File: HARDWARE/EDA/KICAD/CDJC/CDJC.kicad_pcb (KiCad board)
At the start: 2 copper layers, 100 x 100 mm, 55 parts, among them J1 COM_IN, J2 COM_OUT, J3 POWER_IN, J4 POWER_OUT, J5 BIT_OUT, Q1 BC549, SW1 B-SET, U1 74LS04, U2 74LS32, U3 74LS08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

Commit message: pause work0
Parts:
- D10: footprint Diode_THT:D_DO-34_SOD68_P7.62mm_Horizontal -> Diode_THT:D_DO-34_SOD68_P10.16mm_Horizontal
- D11: footprint Diode_THT:D_DO-34_SOD68_P7.62mm_Horizontal -> Diode_THT:D_DO-34_SOD68_P12.70mm_Horizontal
- D20, D21, D9: footprint Diode_THT:D_DO-34_SOD68_P2.54mm_Vertical_AnodeUp -> Diode_THT:D_DO-34_SOD68_P7.62mm_Horizontal
- R10, R12, R13, R14, R15, R16, R7: footprint Resistor_THT:R_Axial_DIN0207_L6.3mm_D2.5mm_P2.54mm_Vertical -> Resistor_THT:R_Axial_DIN0207_L6.3mm_D2.5mm_P7.62mm_Horizontal
- moved U4 46.6 mm to (164.1, 106.8), turned to 270 degrees
- moved U9 44.0 mm to (223.0, 106.2), turned to 270 degrees
- moved D21 38.6 mm to (218.0, 95.9)
- moved SW1 24.5 mm to (124.5, 98.6)
- moved R1 24.5 mm to (128.8, 110.1)
- moved R2 24.5 mm to (128.8, 105.3)
- moved R4 24.5 mm to (130.8, 112.5)
- moved R5 24.5 mm to (130.8, 107.7)
- moved R6 24.5 mm to (130.8, 102.9)
- moved D1 24.5 mm to (123.3, 111.7)
- moved D2 24.5 mm to (123.3, 107.2)
- moved D3 24.5 mm to (123.3, 102.6)
- moved D10 22.2 mm to (208.7, 126.6), turned to 90 degrees
- moved D11 21.6 mm to (225.0, 116.5)
- moved R13 21.3 mm to (177.7, 137.8)
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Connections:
- U4 pad 10: Net-(U1-Pad8) -> Net-(U4-Pad10)
- U4 pad 6: Net-(U4-Pad6) -> Net-(U4-Pad10)
- U4 pad 9: Net-(U4-Pad6) -> Net-(U1-Pad8)
- U7 pad 10: FBMon -> NBMon
- U7 pad 9: NBMon -> FBMon
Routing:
- net LBMon: track 1.04 -> 78.0 mm, vias 0 -> 2
- net +5VD: track 174.2 -> 105.5 mm, vias 6 -> 2
- net Net-(D21-Pad1): track 0.07 -> 61.7 mm
- net LB_SW: track 167.6 -> 120.6 mm, vias 2 -> 4
- net FBMon: track 0.00 -> 46.4 mm, vias 0 -> 2
- net MRLMon: track 0.00 -> 43.6 mm, vias 0 -> 2
- net Net-(U1-Pad8): track 37.5 -> 0.00 mm
- net Net-(U6-Pad3): track 0.00 -> 35.8 mm, vias 0 -> 2
- net NB_SW: track 80.5 -> 45.1 mm, vias 2 -> 0
- net Net-(D16-Pad2): track 0.00 -> 30.2 mm
- net Net-(U5-Pad3): track 0.00 -> 30.0 mm, vias 0 -> 2
- net LBLBI: track 116.8 -> 145.7 mm
- net Net-(U1-Pad4): track 36.9 -> 8.99 mm
- net Net-(D17-Pad2): track 0.00 -> 27.4 mm
- net Net-(D13-Pad1): track 0.00 -> 26.1 mm
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
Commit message: i am crazy
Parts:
- R1, R2, R3, R4, R5, R6: footprint Resistor_THT:R_Axial_DIN0207_L6.3mm_D2.5mm_P2.54mm_Vertical -> Resistor_THT:R_Axial_DIN0207_L6.3mm_D2.5mm_P7.62mm_Horizontal
- moved SW1 67.5 mm to (171.8, 50.4), turned to 270 degrees
- moved R4 58.0 mm to (173.5, 73.2)
- moved R6 58.0 mm to (173.5, 63.6)
- moved R5 58.0 mm to (173.5, 68.4)
- moved R3 54.8 mm to (165.9, 61.2), turned to 0 degrees
- moved D2 54.0 mm to (160.4, 67.9)
- moved R1 54.0 mm to (165.8, 70.8)
- moved R2 54.0 mm to (165.8, 66.0)
- moved D1 54.0 mm to (160.4, 72.4)
- moved D3 54.0 mm to (160.4, 63.3)
- moved U1 32.5 mm to (177.7, 115.4), turned to 90 degrees
- moved U4 15.3 mm to (177.7, 99.9), turned to 90 degrees
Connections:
- U1 pad 11: FB_SW -> NB_SW
- U1 pad 13: NB_SW -> LB_SW
- U1 pad 9: LB_SW -> FB_SW
- U2 pad 12: NB_SW -> LB_SW
- U2 pad 13: LB_SW -> NB_SW
- U2 pad 6: Net-(U1-Pad1) -> Net-(U1-Pad5)
- U2 pad 8: Net-(U1-Pad5) -> Net-(U1-Pad1)
- U3 pad 1: GNDD -> LB_SW
- U3 pad 10: FB_SW -> Net-(D10-Pad1)
- U3 pad 11: LBMon -> FBMon
- U3 pad 12: LB_SW -> FB_SW
- U3 pad 13: Net-(U1-Pad2) -> Net-(U1-Pad4)
- U3 pad 2: GNDD -> Net-(U1-Pad6)
- U3 pad 3: Net-(U3-Pad3) -> LBMon
- U3 pad 4: Net-(U1-Pad6) -> Net-(U1-Pad2)
- U3 pad 8: FBMon -> Net-(U3-Pad8)
- U3 pad 9: Net-(U1-Pad4) -> MRLMon
- U4 pad 4: Net-(U1-Pad12) -> Net-(U1-Pad10)
- U4 pad 5: Net-(U1-Pad10) -> Net-(U1-Pad8)
- U4 pad 9: Net-(U1-Pad8) -> Net-(U1-Pad12)
- U6 pad 1: Net-(D10-Pad1) -> GNDD
- U6 pad 2: MRLMon -> GNDD
- U8 pad 2: Net-(U6-Pad3) -> Net-(U3-Pad8)
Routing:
- net Net-(U1-Pad1): track 0.00 -> 91.0 mm, vias 0 -> 2
- net Net-(U1-Pad3): track 0.00 -> 68.9 mm
- net Net-(U1-Pad6): track 6.98 -> 67.8 mm, vias 0 -> 2
- net Net-(U1-Pad5): track 0.06 -> 56.5 mm
- net Net-(U1-Pad4): track 8.99 -> 63.5 mm, vias 0 -> 2
- net NB_SW: track 45.1 -> 96.6 mm, vias 0 -> 2
- net GNDD: track 208.7 -> 257.7 mm, vias 6 -> 10
- net NBMon: track 15.4 -> 58.0 mm, vias 0 -> 2
- net Net-(U6-Pad3): track 35.8 -> 0.00 mm, vias 2 -> 0
- net LBMon: track 78.0 -> 110.4 mm, vias 2 -> 6
- net Net-(U3-Pad8): track 0.00 -> 25.3 mm, vias 0 -> 2
- net Net-(U1-Pad2): track 26.2 -> 48.1 mm, vias 0 -> 2
- net FB_SW: track 71.9 -> 91.9 mm
- net Net-(U1-Pad12): track 14.2 -> 31.9 mm, vias 0 -> 2
- net Net-(U1-Pad8): track 0.00 -> 9.98 mm
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
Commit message: i am crazy
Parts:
- moved U1 15.9 mm to (193.4, 112.9), turned to 180 degrees
- moved R3 13.9 mm to (152.1, 62.7)
- moved R5 13.9 mm to (159.7, 69.9)
- moved SW1 13.9 mm to (158.0, 51.9)
- moved D1 13.9 mm to (146.6, 73.9)
- moved D2 13.9 mm to (146.6, 69.4)
- moved D3 13.9 mm to (146.6, 64.8)
- moved R1 13.9 mm to (152.1, 72.3)
- moved R2 13.9 mm to (152.1, 67.5)
- moved R4 13.9 mm to (159.7, 74.7)
- moved R6 13.9 mm to (159.7, 65.1)
- moved U4 13.6 mm to (173.4, 112.8), turned to 180 degrees
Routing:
- net LB_SW: track 119.3 -> 28.3 mm, vias 4 -> 0
- net Net-(U1-Pad1): track 91.0 -> 0.00 mm, vias 2 -> 0
- net NB_SW: track 96.6 -> 24.4 mm, vias 2 -> 0
- net Net-(U1-Pad3): track 68.9 -> 0.00 mm
- net Net-(U1-Pad6): track 67.8 -> 0.00 mm, vias 2 -> 0
- net LBMon: track 110.4 -> 45.8 mm, vias 6 -> 2
- net Net-(U1-Pad4): track 63.5 -> 0.00 mm, vias 2 -> 0
- net Net-(U1-Pad5): track 56.5 -> 0.00 mm
- net Net-(U1-Pad2): track 48.1 -> 0.00 mm, vias 2 -> 0
- net MRLMon: track 44.0 -> 0.00 mm
- net NBMon: track 58.0 -> 15.4 mm, vias 2 -> 0
- net Net-(U1-Pad12): track 31.9 -> 0.00 mm, vias 2 -> 0
- net FB_SW: track 91.9 -> 63.9 mm, vias 4 -> 2
- net Net-(U1-Pad8): track 9.98 -> 0.00 mm
- net Net-(U1-Pad10): track 8.93 -> 0.00 mm
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
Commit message: ajdust PCB
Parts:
- moved R5 51.4 mm to (178.4, 117.8)
- moved D1 51.4 mm to (165.3, 121.8)
- moved D2 51.4 mm to (165.3, 117.3)
- moved D3 51.4 mm to (165.3, 112.7)
- moved R1 51.4 mm to (170.8, 120.2)
- moved R2 51.4 mm to (170.8, 115.4)
- moved R3 51.4 mm to (170.8, 110.6)
- moved R4 51.4 mm to (178.4, 122.6)
- moved R6 51.4 mm to (178.4, 113.0)
- moved SW1 48.9 mm to (170.9, 99.1)
- moved U4 43.9 mm to (171.3, 69.0)
- moved U3 36.8 mm to (194.8, 115.8), turned to 180 degrees
- moved U1 25.7 mm to (190.4, 87.4)
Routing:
- net FB_SW: track 63.9 -> 8.67 mm, vias 2 -> 0
- net FBMon: track 56.3 -> 18.2 mm
- net LB_SW: track 28.3 -> 10.3 mm
- net NB_SW: track 24.4 -> 11.9 mm
- net Net-(U3-Pad8): track 25.3 -> 14.5 mm, vias 2 -> 1

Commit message: remaining editions
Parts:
- moved R1 48.0 mm to (167.1, 72.3)
- moved R6 48.0 mm to (174.7, 65.1)
- moved R2 48.0 mm to (167.1, 67.5)
- moved R3 48.0 mm to (167.1, 62.7)
- moved R4 48.0 mm to (174.7, 74.7)
- moved R5 48.0 mm to (174.7, 69.9)
- moved D2 48.0 mm to (162.3, 69.4)
- moved D3 48.0 mm to (162.3, 64.8)
- moved D1 48.0 mm to (162.3, 73.9)
- moved U4 47.6 mm to (172.2, 116.6)
- moved SW1 47.0 mm to (162.6, 52.8), turned to 0 degrees
- moved U2 15.9 mm to (217.9, 89.9), turned to 180 degrees
- moved U1 5.24 mm to (195.0, 89.9)
- moved D4 2.60 mm to (162.7, 133.9)
- moved D5 2.60 mm to (162.7, 130.2)
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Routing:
- net GNDD: track 257.7 -> 230.4 mm, vias 10 -> 8
- net Net-(U5-Pad10): track 42.8 -> 41.8 mm
- net Net-(U6-Pad6): track 45.4 -> 44.6 mm
- net Net-(D1-Pad2): track 2.78 -> 3.61 mm
- net Net-(U6-Pad10): track 27.3 -> 26.7 mm

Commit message: adjusts in PCB
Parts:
- moved U2 71.1 mm to (146.8, 88.8), turned to 0 degrees
- moved U3 35.0 mm to (173.5, 88.9), turned to 0 degrees
- moved U1 34.9 mm to (160.1, 88.8), turned to 0 degrees
- moved U4 31.5 mm to (187.2, 88.9), turned to 0 degrees
- moved D1 1.97 mm to (162.2, 72.0)
- moved R3 1.97 mm to (167.0, 60.7)
- moved R5 1.97 mm to (174.6, 67.9)
- moved D2 1.97 mm to (162.2, 67.4)
- moved R1 1.97 mm to (167.0, 70.3)
- moved R2 1.97 mm to (167.0, 65.5)
- moved R4 1.97 mm to (174.7, 72.7)
- moved R6 1.97 mm to (174.7, 63.1)
- moved D3 1.97 mm to (162.2, 62.9)
- moved SW1 1.38 mm to (162.5, 51.4)
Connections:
- U1 pad 1: Net-(U1-Pad1) -> NB_SW
- U1 pad 11: NB_SW -> Net-(U1-Pad11)
- U1 pad 13: LB_SW -> FB_SW
- U1 pad 5: Net-(U1-Pad5) -> LB_SW
- U1 pad 9: FB_SW -> Net-(U1-Pad9)
- U2 pad 6: Net-(U1-Pad5) -> Net-(U1-Pad9)
- U2 pad 8: Net-(U1-Pad1) -> Net-(U1-Pad11)
- U3 pad 1: LB_SW -> NB_SW
- U3 pad 10: Net-(D10-Pad1) -> Net-(U1-Pad12)
- U3 pad 2: Net-(U1-Pad6) -> Net-(U1-Pad10)
- U3 pad 3: LBMon -> NBMon
- U3 pad 4: Net-(U1-Pad2) -> Net-(U1-Pad8)
- U3 pad 5: NB_SW -> LB_SW
- U3 pad 6: NBMon -> LBMon
- U3 pad 9: MRLMon -> Net-(U1-Pad2)
- U4 pad 1: FB_SW -> NB_SW
- U4 pad 11: MRLMon -> Net-(U4-Pad11)
- U4 pad 12: Net-(U4-Pad12) -> MRLMon
- U4 pad 13: LB_SW -> Net-(D10-Pad1)
- U4 pad 2: NB_SW -> FB_SW
- U4 pad 3: Net-(U4-Pad12) -> Net-(U4-Pad10)
- U4 pad 4: Net-(U1-Pad10) -> Net-(U1-Pad6)
- U4 pad 5: Net-(U1-Pad8) -> Net-(U3-Pad8)
- U4 pad 6: Net-(U4-Pad10) -> ELMon
- U4 pad 8: ELMon -> MRLMon
- U4 pad 9: Net-(U1-Pad12) -> LB_SW
- U8 pad 2: Net-(U3-Pad8) -> Net-(U4-Pad11)
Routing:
- net LB_SW: track 10.3 -> 110.5 mm, vias 0 -> 4
- net FB_SW: track 8.67 -> 92.3 mm
- net +5VD: track 100.7 -> 171.5 mm, vias 2 -> 8
- net NB_SW: track 11.9 -> 70.4 mm, vias 0 -> 4
- net Net-(U1-Pad6): track 0.00 -> 55.9 mm, vias 0 -> 2
- net Net-(U1-Pad2): track 0.00 -> 53.2 mm, vias 0 -> 4
- net Net-(U1-Pad4): track 0.00 -> 41.6 mm, vias 0 -> 2
- net Net-(U1-Pad9): track 0.00 -> 35.1 mm
- net Net-(U1-Pad12): track 0.00 -> 32.0 mm
- net Net-(U1-Pad11): track 0.00 -> 28.7 mm
- net NBMon: track 15.4 -> 32.6 mm
- net Net-(U4-Pad11): track 0.00 -> 14.5 mm, vias 0 -> 1
- net Net-(U1-Pad8): track 0.00 -> 11.3 mm
- net Net-(U4-Pad10): track 0.00 -> 11.1 mm
- net Net-(U1-Pad10): track 0.00 -> 10.7 mm
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
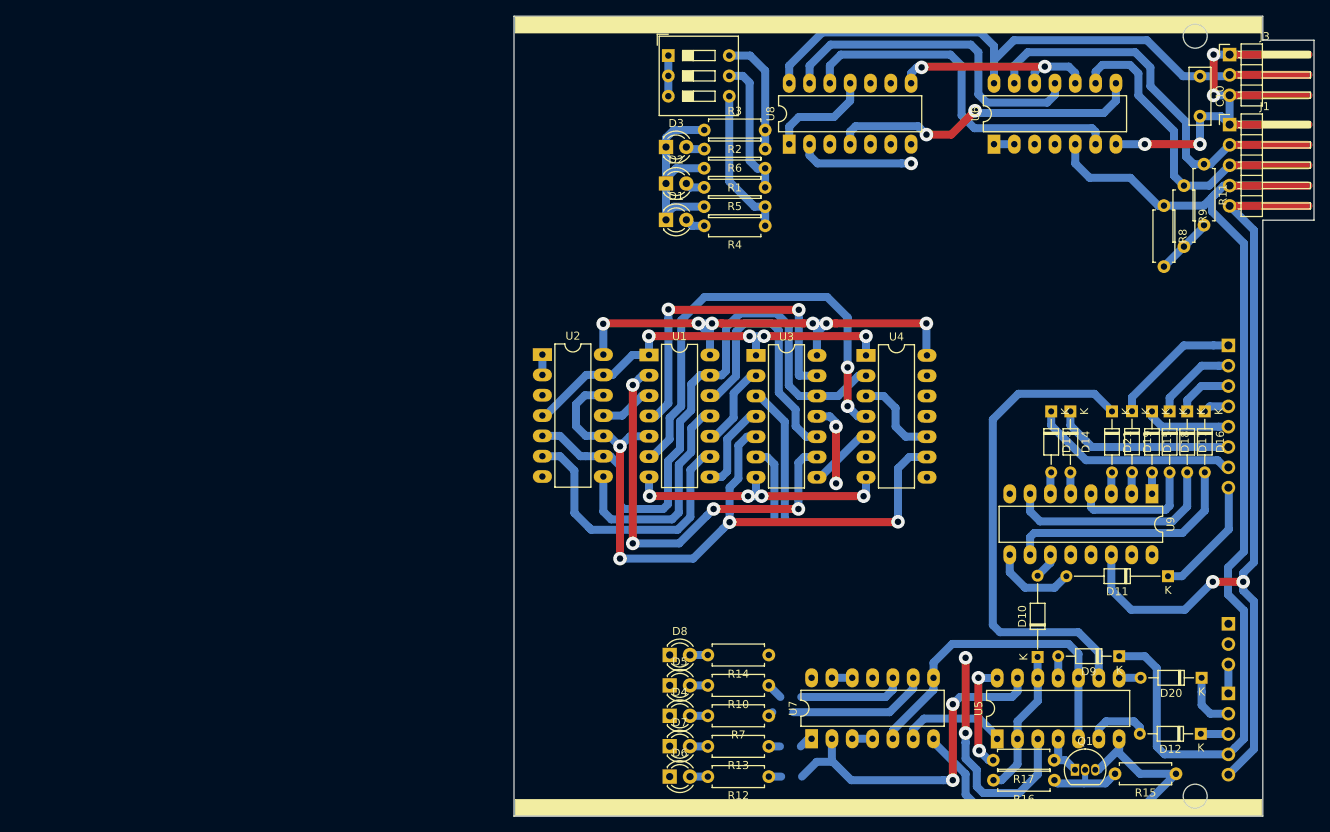
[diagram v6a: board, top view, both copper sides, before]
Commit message: Re-associate footprints by reference
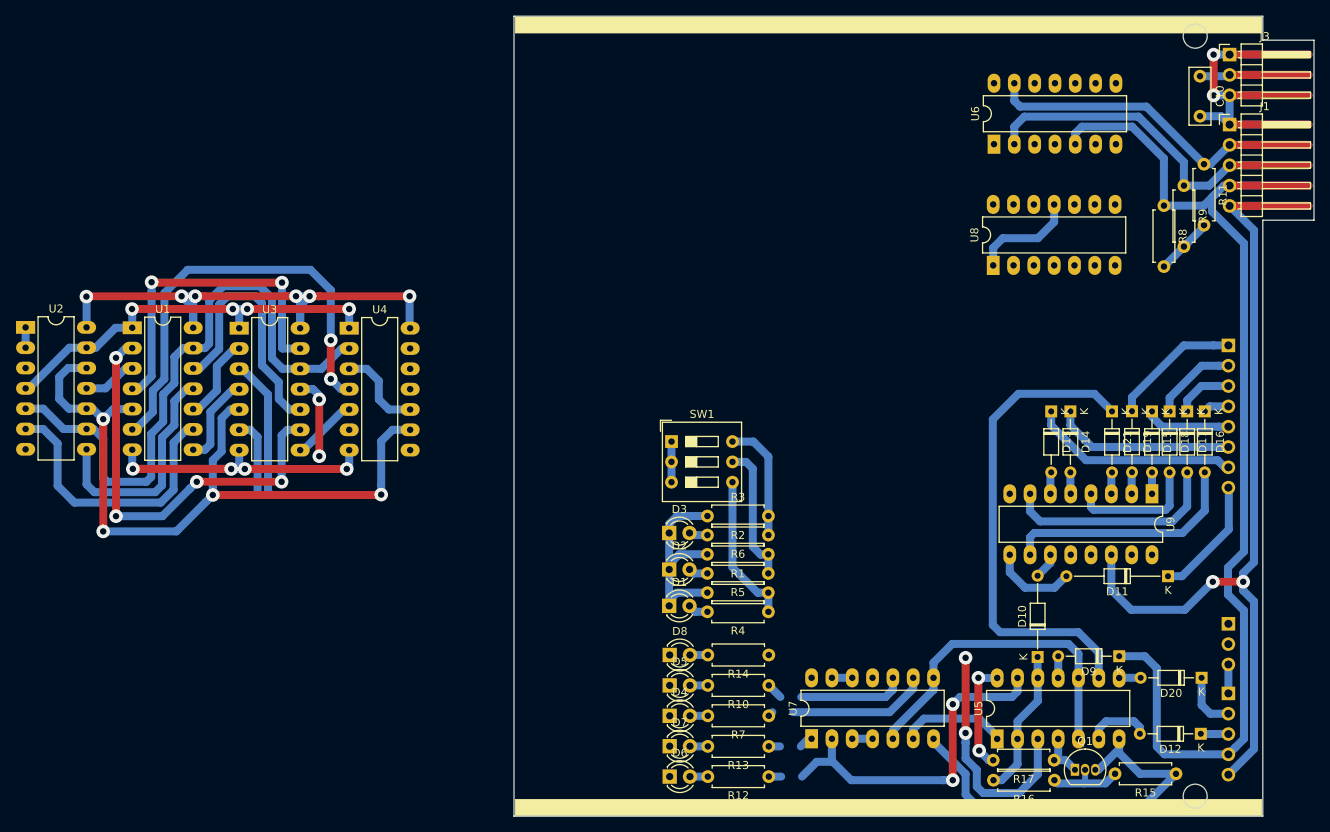
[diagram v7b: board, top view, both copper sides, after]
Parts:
- moved U2 64.7 mm to (82.2, 85.4)
- moved U1 64.7 mm to (95.5, 85.5)
- moved U3 64.7 mm to (108.9, 85.5)
- moved U4 64.7 mm to (122.7, 85.5)
- moved R3 48.3 mm to (167.4, 109.0)
- moved D1 48.3 mm to (162.7, 120.2)
- moved D2 48.3 mm to (162.7, 115.7)
- moved R1 48.3 mm to (167.4, 118.6)
- moved R2 48.3 mm to (167.4, 113.8)
- moved R4 48.3 mm to (175.1, 121.0)
- moved R5 48.3 mm to (175.0, 116.2)
- moved R6 48.3 mm to (175.1, 111.4)
- moved SW1 48.3 mm to (162.9, 99.7)
- moved D3 48.3 mm to (162.7, 111.1)
- moved U8 29.7 mm to (203.2, 77.7)
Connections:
- U6 pad 1: GNDD -> Net-(U6-Pad1)
- U6 pad 10: Net-(U6-Pad10) -> GNDD
- U6 pad 12: Net-(U6-Pad10) -> Net-(U6-Pad1)
- U6 pad 2: GNDD -> EI
- U6 pad 9: EI -> GNDD
- U8 pad 4: Net-(U6-Pad8) -> Net-(U6-Pad3)
- U8 pad 8: Net-(U6-Pad10) -> Net-(U6-Pad1)
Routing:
- net +5VD: track 171.5 -> 108.0 mm
- net Net-(U6-Pad6): track 45.2 -> 0.07 mm
- net Net-(U6-Pad11): track 42.1 -> 0.17 mm
- net Net-(U6-Pad8): track 39.7 -> 0.00 mm, vias 2 -> 0
- net Net-(U6-Pad10): track 26.7 -> 0.00 mm, vias 2 -> 0
- net GNDD: track 223.5 -> 207.0 mm, vias 8 -> 6
- net Net-(U4-Pad11): track 14.5 -> 0.00 mm, vias 1 -> 0
- net MRI: track 60.2 -> 53.1 mm
- net EI: track 50.4 -> 55.7 mm
- net LBLBI: track 143.3 -> 148.0 mm

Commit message: Re-associate footprints by reference
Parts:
- moved U8 0.10 mm to (203.2, 77.7)
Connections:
- U8 pad 1: Net-(U8-Pad1) -> Net-(U6-Pad3)
- U8 pad 10: LBMon -> Net-(U6-Pad11)
- U8 pad 11: Net-(U8-Pad1) -> Net-(U6-Pad1)
- U8 pad 12: Net-(U6-Pad6) -> LBMon
- U8 pad 13: Net-(U6-Pad11) -> NBMon
- U8 pad 2: Net-(U4-Pad11) -> Net-(U5-Pad3)
- U8 pad 4: Net-(U6-Pad3) -> Net-(U4-Pad11)
- U8 pad 5: Net-(U5-Pad3) -> Net-(U8-Pad5)
- U8 pad 8: Net-(U6-Pad1) -> Net-(U8-Pad5)
- U8 pad 9: NBMon -> Net-(U6-Pad6)
- U9 pad 13: Net-(U8-Pad6) -> Net-(U8-Pad3)
- U9 pad 15: Net-(U8-Pad3) -> Net-(U8-Pad6)
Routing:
- net Net-(U8-Pad1): track 13.4 -> 0.00 mm
